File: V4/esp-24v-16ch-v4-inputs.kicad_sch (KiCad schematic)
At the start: 10 parts, among them U10 OR-3H7-4

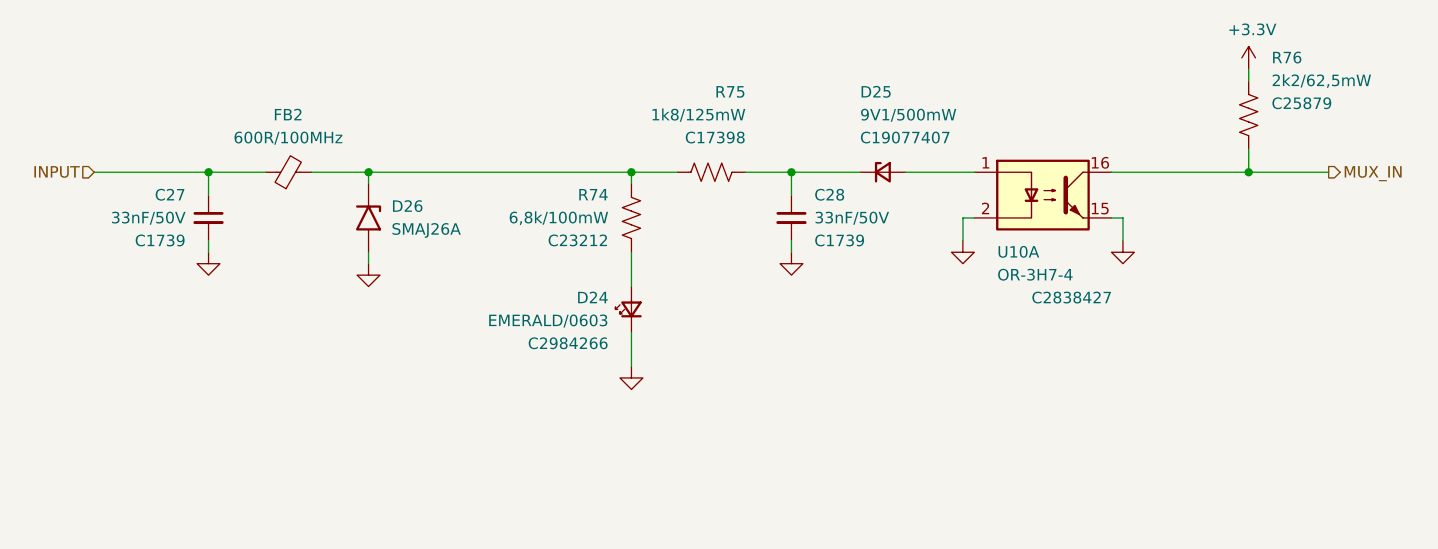
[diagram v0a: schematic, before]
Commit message: Updating PCB for V4
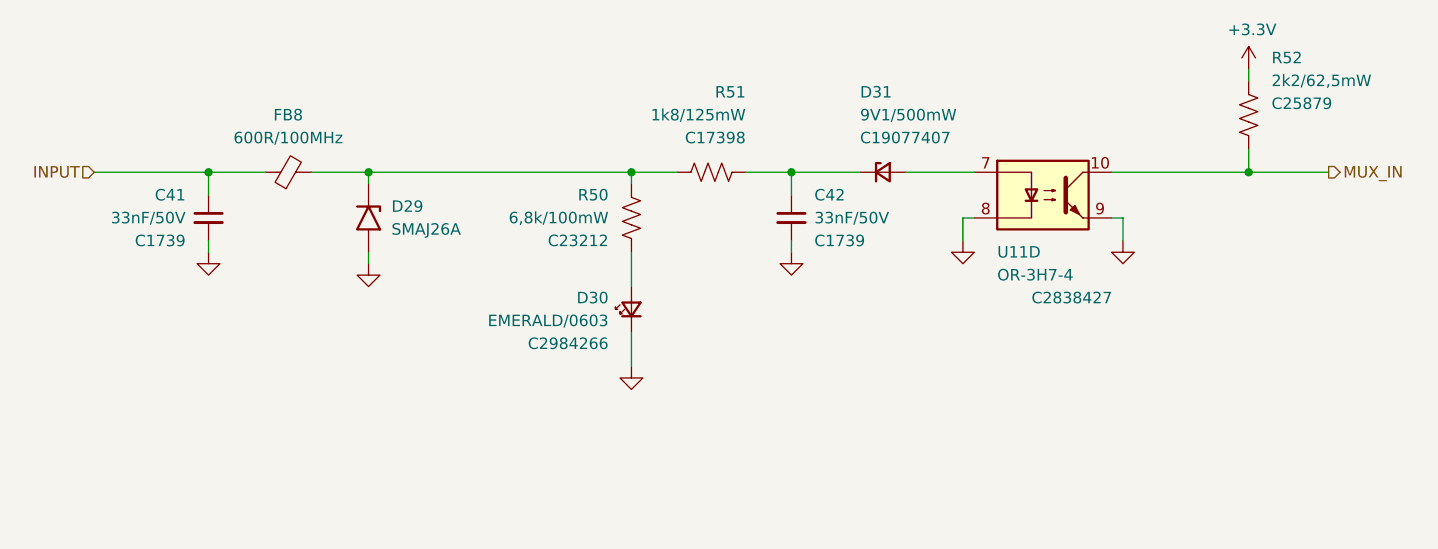
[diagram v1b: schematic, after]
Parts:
- renumbered C27 to C41, C28 to C42, D26 to D29, D24 to D30, D25 to D31, FB2 to FB8, R74 to R50, R75 to R51, R76 to R52, U10 to U11
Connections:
- net GND: now also U11.8, U11.9; no longer U11.15, U11.2
- net MUX_IN: now also U11.10; no longer U11.16
- net at D31.2 (A): now also U11.7; no longer U11.1

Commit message: Routing V4
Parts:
- C41: value 33nF/50V -> 1nF/50V; footprint Tales:C_0805_2012Metric -> Tales:C_0603_1608Metric; Case 0805/2012 -> 0603/1608; LCSC Part # C1739 -> C1588; Mfr FH -> Samsung; Mfr PN 0805B333K500NT -> CL10B102KB8NNNC; Technology Ceramic -> Ceramic X7R; Vendor PN C1739 -> C1588
- C42: footprint Tales:C_0805_2012Metric -> Tales:C_0603_1608Metric; Case 0805/2012 -> 0603/1608; LCSC Part # C1739 -> C21117; Mfr FH -> Samsung; Mfr PN 0805B333K500NT -> CL10B333KB8NNNC; Technology Ceramic -> Ceramic X7R; Vendor PN C1739 -> C21117
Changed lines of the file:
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@@
 			)
 		)
-		(property "Footprint" "Tales:C_0805_2012Metric"
+		(property "Footprint" "Tales:C_0603_1608Metric"
 			(at 143.51 97.79 0)
 			(effects
@@
 			)
 		)
-		(property "Technology" "Ceramic"
+		(property "Technology" "Ceramic X7R"
 			(at 143.51 97.79 0)
 			(effects
@@
 			)
 		)
-		(property "Case" "0805/2012"
+		(property "Case" "0603/1608"
 			(at 143.51 97.79 0)
 			(effects
@@
 			)
 		)
-		(property "Mfr" "FH"
+		(property "Mfr" "Samsung"
 			(at 143.51 97.79 0)
 			(effects
@@
 			)
 		)
-		(property "Mfr PN" "0805B333K500NT"
+		(property "Mfr PN" "CL10B333KB8NNNC"
 			(at 143.51 97.79 0)
 			(effects
@@
 			)
 		)
-		(property "Vendor PN" "C1739"
+		(property "Vendor PN" "C21117"
 			(at 143.51 97.79 0)
 			(effects
@@
 			)
 		)
-		(property "LCSC Part #" "C1739"
+		(property "LCSC Part #" "C21117"
 			(at 146.05 100.3362 0)
 			(effects
@@
 		(fields_autoplaced yes)
 		(property "Reference" "C41"
-			(at 76.2 95.2562 0)
-			(effects
-				(font
-					(size 1.27 1.27)
-				)
-				(justify right)
-			)
-		)
-		(property "Value" "33nF/50V"
-			(at 76.2 97.7962 0)
-			(effects
-				(font
-					(size 1.27 1.27)
-				)
-				(justify right)
-			)
-		)
-		(property "Footprint" "Tales:C_0805_2012Metric"
+			(at 81.28 95.2562 0)
+			(effects
+				(font
+					(size 1.27 1.27)
+				)
+				(justify left)
+			)
+		)
+		(property "Value" "1nF/50V"
+			(at 81.28 97.7962 0)
+			(effects
+				(font
+					(size 1.27 1.27)
+				)
+				(justify left)
+			)
+		)
+		(property "Footprint" "Tales:C_0603_1608Metric"
 			(at 78.74 97.79 0)
 			(effects
@@
 			)
 		)
-		(property "Technology" "Ceramic"
+		(property "Technology" "Ceramic X7R"
 			(at 78.74 97.79 0)
 			(effects
@@
 			)
 		)
-		(property "Case" "0805/2012"
+		(property "Case" "0603/1608"
 			(at 78.74 97.79 0)
 			(effects
@@
 			)
 		)
-		(property "Mfr" "FH"
+		(property "Mfr" "Samsung"
 			(at 78.74 97.79 0)
 			(effects
@@
 			)
 		)
-		(property "Mfr PN" "0805B333K500NT"
+		(property "Mfr PN" "CL10B102KB8NNNC"
 			(at 78.74 97.79 0)
 			(effects
@@
 			)
 		)
-		(property "Vendor PN" "C1739"
+		(property "Vendor PN" "C1588"
 			(at 78.74 97.79 0)
 			(effects
@@
 			)
 		)
-		(property "LCSC Part #" "C1739"
-			(at 76.2 100.3362 0)
-			(effects
-				(font
-					(size 1.27 1.27)
-				)
-				(justify right)
-			)
-		)
+		(property "LCSC Part #" "C1588"
+			(at 81.28 100.3362 0)
+			(effects
+				(font
+					(size 1.27 1.27)
+				)
+				(justify left)
+			)
+		)

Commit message: Routing V4
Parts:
- D29: now not fitted; now left out of the parts list
- D30: value EMERALD/0603 -> WHITE/0603; LCSC Part # C2984266 -> C2290; Mfr Everlight Elec -> Hubei KENTO Elec; Mfr PN 19-213/GHC-XS1T1N/5T -> KT-0603W; Vendor PN C2984266 -> C2290
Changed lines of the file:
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@@
 		(unit 1)
 		(exclude_from_sim no)
-		(in_bom yes)
-		(on_board yes)
-		(dnp no)
+		(in_bom no)
+		(on_board no)
+		(dnp yes)
 		(fields_autoplaced yes)
 		(property "Reference" "D29"
@@
 			)
 		)
-		(property "Value" "EMERALD/0603"
+		(property "Value" "WHITE/0603"
 			(at 123.19 109.22 90)
 			(effects
@@
 			)
 		)
-		(property "Mfr" "Everlight Elec"
+		(property "Mfr" "Hubei KENTO Elec"
 			(at 125.73 107.95 0)
 			(effects
@@
 			)
 		)
-		(property "Mfr PN" "19-213/GHC-XS1T1N/5T"
+		(property "Mfr PN" "KT-0603W"
 			(at 125.73 107.95 0)
 			(effects
@@
 			)
 		)
-		(property "Vendor PN" "C2984266"
+		(property "Vendor PN" "C2290"
 			(at 125.73 107.95 0)
 			(effects
@@
 			)
 		)
-		(property "LCSC Part #" "C2984266"
+		(property "LCSC Part #" "C2290"
 			(at 123.19 111.76 90)
 			(effects

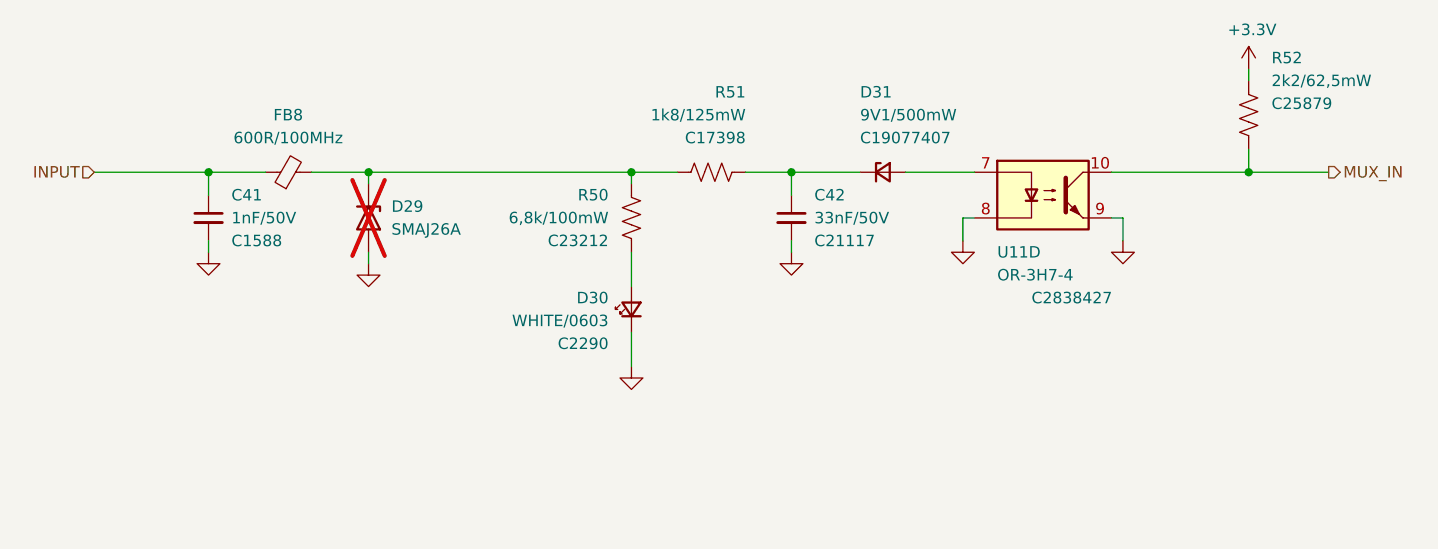
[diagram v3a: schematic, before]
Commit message: Upgrade to Kicad 9
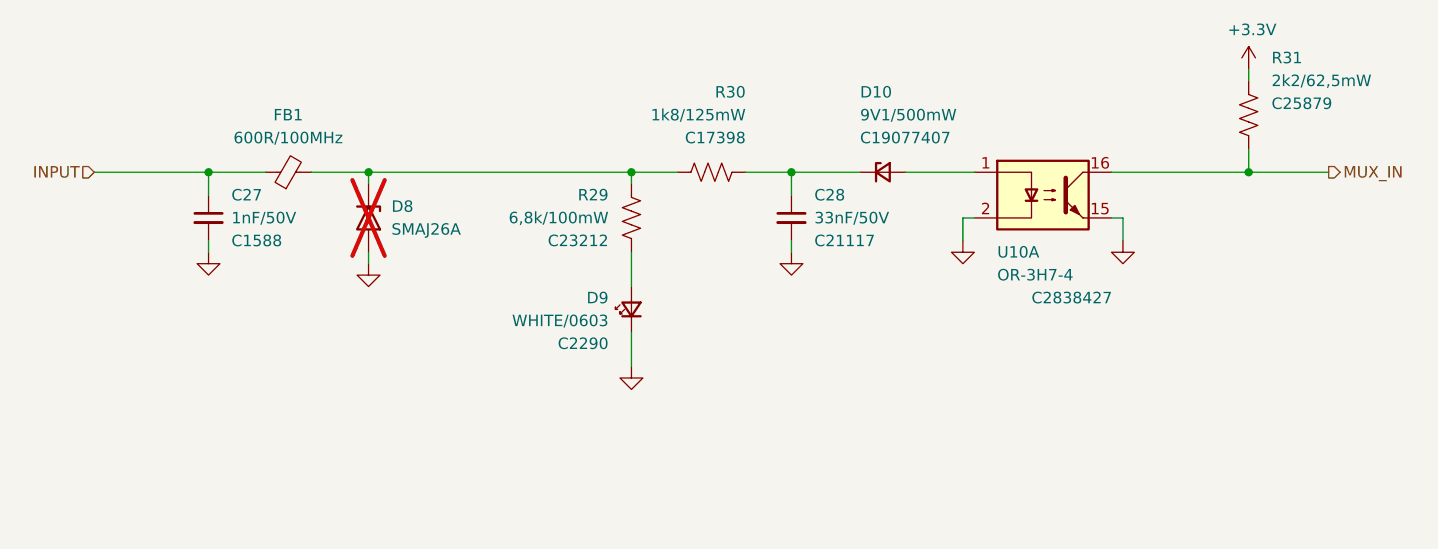
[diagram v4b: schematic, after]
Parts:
- renumbered C41 to C27, C42 to C28, D31 to D10, D29 to D8, D30 to D9, FB8 to FB1, R50 to R29, R51 to R30, R52 to R31, U11 to U10
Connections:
- net GND: now also U10.15, U10.2; no longer U10.8, U10.9
- net MUX_IN: now also U10.16; no longer U10.10
- net at D10.2 (A): now also U10.1; no longer U10.7
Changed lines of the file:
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@@
 (kicad_sch
-	(version 20231120)
+	(version 20250114)
 	(generator "eeschema")
-	(generator_version "8.0")
+	(generator_version "9.0")
 	(paper "A4")
 	(junction
@@
 		(shape input)
 		(at 66.04 92.71 180)
-		(fields_autoplaced yes)
 		(effects
 			(font
@@
 		(shape output)
 		(at 203.2 92.71 0)
-		(fields_autoplaced yes)
 		(effects
 			(font
@@
 		(on_board yes)
 		(dnp no)
-		(property "Reference" "R51"
+		(property "Reference" "R30"
 			(at 138.43 83.82 90)
 			(effects
@@
 		(on_board yes)
 		(dnp no)
-		(property "Reference" "#PWR0138"
+		(property "Reference" "#PWR089"
 			(at 125.73 120.65 0)
 			(effects
@@
 		(on_board yes)
 		(dnp no)
-		(property "Reference" "#PWR0136"
+		(property "Reference" "#PWR087"
 			(at 78.74 107.95 0)
 			(effects
@@
 		(dnp no)
 		(fields_autoplaced yes)
-		(property "Reference" "FB8"
+		(property "Reference" "FB1"
 			(at 87.5919 86.36 90)
 			(effects
@@
 		(dnp yes)
 		(fields_autoplaced yes)
-		(property "Reference" "D29"
+		(property "Reference" "D8"
 			(at 99.06 96.5199 90)
 			(effects
@@
 		(dnp no)
 		(fields_autoplaced yes)
-		(property "Reference" "C42"
+		(property "Reference" "C28"
 			(at 146.05 95.2562 0)
 			(effects
@@
 		(on_board yes)
 		(dnp no)
-		(property "Reference" "#PWR0140"
+		(property "Reference" "#PWR091"
 			(at 162.56 106.68 0)
 			(effects
@@
 		(on_board yes)
 		(dnp no)
-		(property "Reference" "D30"
+		(property "Reference" "D9"
 			(at 123.19 106.68 90)
 			(effects
@@
 		(on_board yes)
 		(dnp no)
-		(property "Reference" "D31"
+		(property "Reference" "D10"
 			(at 151.13 83.82 0)
 			(effects
@@
 		(on_board yes)
 		(dnp no)
-		(property "Reference" "#PWR0142"
+		(property "Reference" "#PWR093"
 			(at 194.31 85.09 0)
 			(effects
@@
 		(on_board yes)
 		(dnp no)
-		(property "Reference" "R52"
+		(property "Reference" "R31"
 			(at 196.85 80.01 0)
 			(effects
@@
 		(on_board yes)
 		(dnp no)
-		(property "Reference" "#PWR0139"
+		(property "Reference" "#PWR090"
 			(at 143.51 107.95 0)
 			(effects
@@
 		(dnp no)
 		(fields_autoplaced yes)
-		(property "Reference" "C41"
+		(property "Reference" "C27"
 			(at 81.28 95.2562 0)
 			(effects
@@
 		(on_board yes)
 		(dnp no)
-		(property "Reference" "#PWR0141"
+		(property "Reference" "#PWR092"
 			(at 180.34 106.68 0)
 			(effects
@@
 		(on_board yes)
 		(dnp no)
-		(property "Reference" "#PWR0137"
+		(property "Reference" "#PWR088"
 			(at 96.52 109.22 0)
 			(effects
@@
 		(lib_id "Tales:OR-3H7-4")
 		(at 171.45 95.25 0)
-		(unit 4)
+		(unit 1)
 		(exclude_from_sim no)
 		(in_bom yes)
 		(on_board yes)
 		(dnp no)
-		(property "Reference" "U11"
+		(property "Reference" "U10"
 			(at 166.37 101.6 0)
 			(effects
@@
 		(on_board yes)
 		(dnp no)
-		(property "Reference" "R50"
+		(property "Reference" "R29"
 			(at 123.19 95.25 0)
 			(effects

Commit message: Updated to 2 NTCs instead of 4.
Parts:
- R29, R30, R31: Technology (none) -> 1%
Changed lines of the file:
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@@
 			)
 		)
-		(property "Technology" "~"
+		(property "Technology" "1%"
 			(at 134.62 92.71 0)
 			(effects
@@
 			)
 		)
-		(property "Description" ""
+		(property "Description" "Light emitting diode, small symbol"
 			(at 125.73 107.95 0)
 			(effects
@@
 		)
 		(property "JLCPCB BOM" "1"
+			(at 125.73 107.95 0)
+			(effects
+				(font
+					(size 1.27 1.27)
+				)
+				(hide yes)
+			)
+		)
+		(property "Sim.Pin" "1=K 2=A"
 			(at 125.73 107.95 0)
 			(effects
@@
 			)
 		)
-		(property "Technology" "~"
+		(property "Technology" "1%"
 			(at 194.31 86.36 0)
 			(effects
@@
 			)
 		)
-		(property "Technology" "~"
+		(property "Technology" "1%"
 			(at 125.73 97.79 0)
 			(effects

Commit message: Created release for V4.0
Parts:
- D8: footprint Tales:D_SMA -> Diode_SMD:D_SMA
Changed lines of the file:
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@@
 			)
 		)
-		(property "Description" ""
+		(property "Description" "Resistor, US symbol"
 			(at 134.62 92.71 0)
 			(effects
@@
 			)
 		)
-		(property "Footprint" "Tales:D_SMA"
+		(property "Footprint" "Diode_SMD:D_SMA"
 			(at 91.44 97.79 0)
 			(effects
@@
 			)
 		)
-		(property "Description" ""
+		(property "Description" "Unpolarized capacitor, small symbol"
 			(at 143.51 97.79 0)
 			(effects
@@
 			)
 		)
-		(property "Description" ""
+		(property "Description" "Zener diode, small symbol"
 			(at 153.67 92.71 0)
 			(effects
@@
 			)
 		)
-		(property "Description" ""
+		(property "Description" "Resistor, US symbol"
 			(at 194.31 86.36 0)
 			(effects
@@
 			)
 		)
-		(property "Description" ""
+		(property "Description" "Unpolarized capacitor, small symbol"
 			(at 78.74 97.79 0)
 			(effects
@@
 			)
 		)
-		(property "Description" ""
+		(property "Description" "Resistor, US symbol"
 			(at 125.73 97.79 0)
 			(effects

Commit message: Version 4.1
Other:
- note added: "I_{LED} = (24V - V_{LED}) / 6.8k I_{LED} = (24V - 2.7V) / 6.8k I_{LED} = 3,13 mA"
- title: (none) -> ESP 24V 16xIn/16xOut/4xNTC Module
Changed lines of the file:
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@@
 	(generator_version "9.0")
 	(paper "A4")
+	(title_block
+		(title "ESP 24V 16xIn/16xOut/4xNTC Module")
+		(date "2025-07-04")
+		(rev "V4")
+	)
+	(text "I_{LED} = (24V - V_{LED}) / 6.8k\nI_{LED} = (24V - 2.7V) / 6.8k\nI_{LED} = 3,13 mA"
+		(exclude_from_sim no)
+		(at 106.68 132.08 0)
+		(effects
+			(font
+				(size 1.5 1.5)
+			)
+			(justify left bottom)
+		)
+	)
 	(junction
 		(at 96.52 92.71)
